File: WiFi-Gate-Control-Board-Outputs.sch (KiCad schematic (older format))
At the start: 47 parts, among them J10 Screw_Terminal_01x02, J11 Screw_Terminal_01x04, J12 Screw_Terminal_01x04, U24 LMZ21700, U25 LP5024, U26 TCA6408A, U27 ITS4075Q

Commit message: Rev 1.0 Release
Added input design and calculations. Added BOM. Added Fuse 3D Model.
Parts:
- C55: renamed from C72; Description CAP, 0603, 1000pF, 10%, X7R, 10V -> CAP, 0603, 1nF, 10%, X7R, 10V
- C56: renamed from C73; Description CAP, 0603, 1000pF, 10%, X7R, 10V -> CAP, 0603, 1nF, 10%, X7R, 10V
- C59: renamed from C76; Description CAP, 0603, 3300pF, 5%, X7R, 10V -> CAP, 0603, 3.3nF, 5%, X7R, 10V
- J9: renamed from J10; Description CON, THT, 5.08mm Pluggable Terminal Strip, 4 Pos -> CON, THT, 5.08mm Pluggable Terminal Strip, 2 Pos
- RL1, RL2: Vendor Part Number 849-CPC1511 -> 849-CPC1511Y
- renumbered C71 to C54, C74 to C57, C75 to C58, C77 to C60, C78 to C61, C79 to C62, C80 to C63, D14 to D13, D15 to D14, D16 to D15, D17 to D16, D18 to D17, D19 to D18, D20 to D19, D21 to D20, D22 to D21, D23 to D22, D24 to D23, D25 to D24, D26 to D25, D27 to D26, D28 to D27, J11 to J10, J12 to J11, R75 to R63, R76 to R64, R77 to R65, R78 to R66, R79 to R67, R80 to R68, R81 to R69, R82 to R70, R83 to R71, R84 to R72, R85 to R73, R86 to R74, U24 to U21, U25 to U22, U26 to U23, U27 to U24

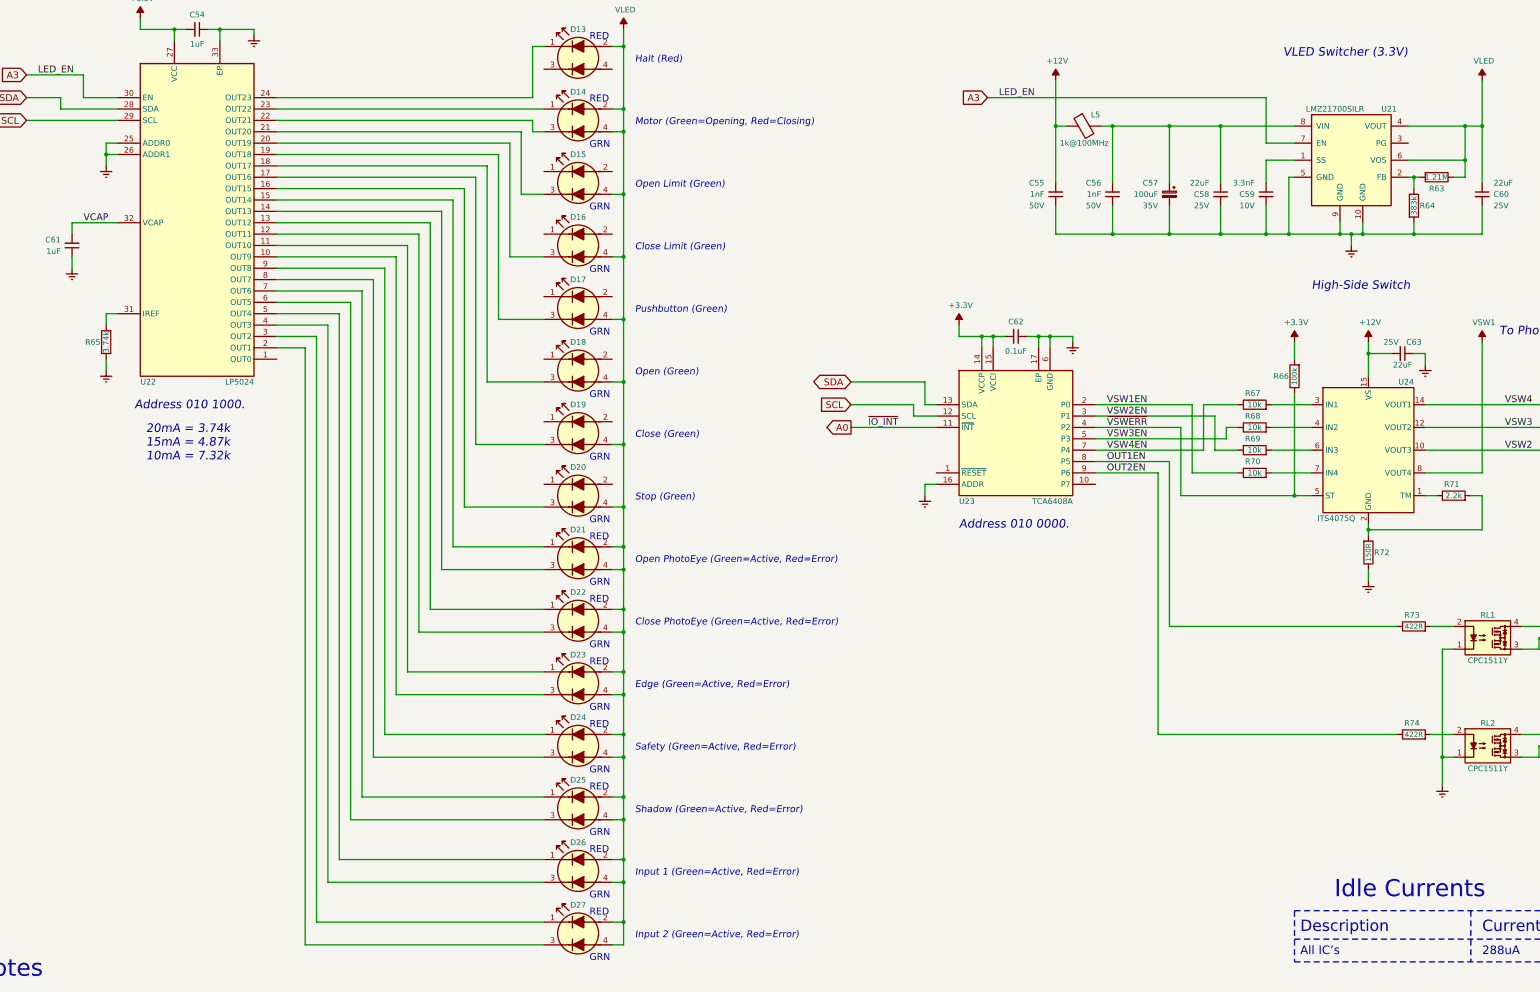
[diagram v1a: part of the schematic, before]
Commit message: PCB to Rev 1.1
Fixed missing Reference Designators on top Silkscreen.
Reset input on TCA6424A and TCA6408A now connected to 3.3V.
Added series Schottky Diode to LED power supply input.
Replaced 1000uF main power capacitor with two 470uF capacitors.
Replaced DS18B20 temperature sensor with TMP100 temperature sensor.
Increased LED currents to 25mA
Removed U26 inverter and connected U3 IN pin directly to processor. Now able to measure unloaded offset current.
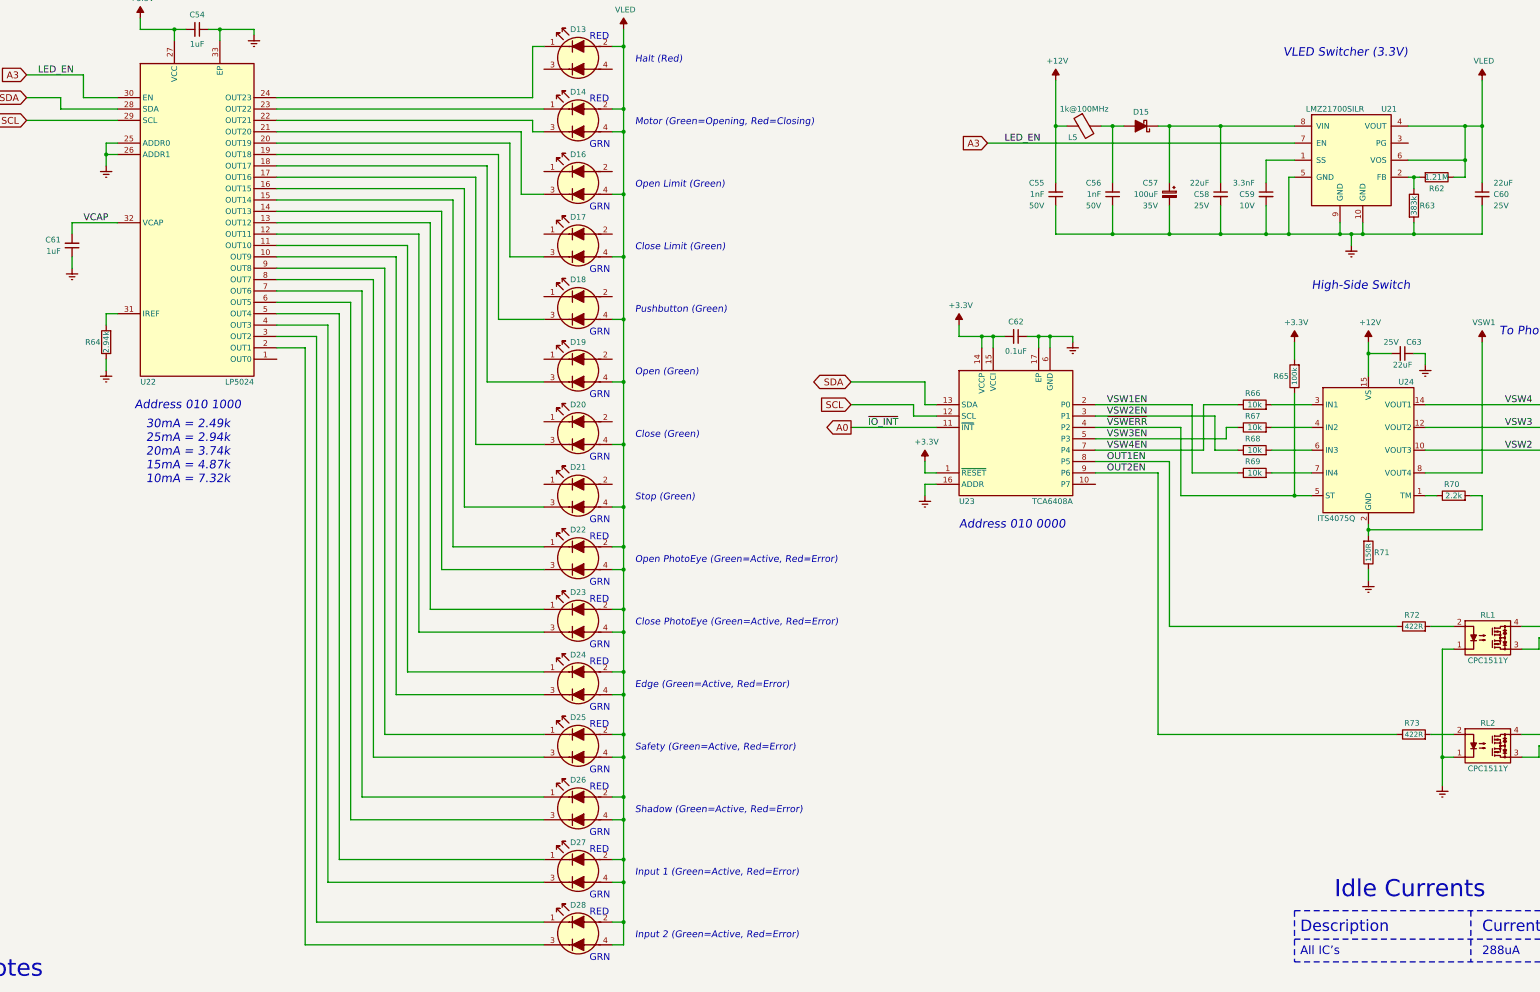
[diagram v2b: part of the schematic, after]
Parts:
- added D15: DFLS130, Diode_SMD:D_PowerDI-123, symbol Device:D_Schottky_ALT
- J10, J11: value Screw_Terminal_01x04 -> Screw Header 4 Pos; Description CON, THT, 5.08mm Pluggable Terminal Strip, 4 Pos -> CON, THT, 5.08mm Pluggable Terminal Header, 4 Pos
- J9: value Screw_Terminal_01x02 -> Screw Header 2 Pos; Description CON, THT, 5.08mm Pluggable Terminal Strip, 2 Pos -> CON, THT, 5.08mm Pluggable Terminal Header, 2 Pos
- R64: renamed from R65; value 3.74k -> 2.94k; Description RES, 0603, 3.74k, 1/10W, 1%, T100 -> RES, 0603, 2.94k, 1/10W, 1%, T100; Part Number ERJ-3EKF3741V -> ERJ-3EKF2941V; Vendor Part Number 667-ERJ-3EKF3741V -> 667-ERJ-3EKF2941V
- R66: renamed from R67; Description RES, 0603, 10k, 1/10W, 1%, T100 -> RES, 0603, 10k, 1/16W, 0.5%, T25; Manufacturer Panasonic -> Susumu; Part Number ERJ-3EKF1002V -> RR0816P-103-D; Tolerance 1% -> 0.5%; Vendor Part Number 667-ERJ-3EKF1002V -> 754-RR0816P-103D
- R67: renamed from R68; Description RES, 0603, 10k, 1/10W, 1%, T100 -> RES, 0603, 10k, 1/16W, 0.5%, T25; Manufacturer Panasonic -> Susumu; Part Number ERJ-3EKF1002V -> RR0816P-103-D; Tolerance 1% -> 0.5%; Vendor Part Number 667-ERJ-3EKF1002V -> 754-RR0816P-103D
- R68: renamed from R69; Description RES, 0603, 10k, 1/10W, 1%, T100 -> RES, 0603, 10k, 1/16W, 0.5%, T25; Manufacturer Panasonic -> Susumu; Part Number ERJ-3EKF1002V -> RR0816P-103-D; Tolerance 1% -> 0.5%; Vendor Part Number 667-ERJ-3EKF1002V -> 754-RR0816P-103D
- R69: renamed from R70; Description RES, 0603, 10k, 1/10W, 1%, T100 -> RES, 0603, 10k, 1/16W, 0.5%, T25; Manufacturer Panasonic -> Susumu; Part Number ERJ-3EKF1002V -> RR0816P-103-D; Tolerance 1% -> 0.5%; Vendor Part Number 667-ERJ-3EKF1002V -> 754-RR0816P-103D
- R70: renamed from R71; Part Number ERJ-3EKF2202V -> ERJ-3EKF2201V; Vendor Part Number 667-ERJ-3EKF2202V -> 667-ERJ-3EKF2201V
- R72: renamed from R73; Description RES, 0603, 42R, 1/10W, 1%, T100 -> RES, 0603, 422R, 1/10W, 1%, T100
- R73: renamed from R74; Description RES, 0603, 42R, 1/10W, 1%, T100 -> RES, 0603, 422R, 1/10W, 1%, T100
- renumbered D15 to D16, D16 to D17, D17 to D18, D18 to D19, D19 to D20, D20 to D21, D21 to D22, D22 to D23, D23 to D24, D24 to D25, D25 to D26, D26 to D27, D27 to D28, R63 to R62, R64 to R63, R66 to R65, R72 to R71
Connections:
- net +3.3V: now also U23.1 (~RESET)
- net at C57.1, C58.1, U21.8 (VIN): now also D15.1 (K); no longer C56.2, L5.2
- new net: C56.2, D15.2 (A), L5.2
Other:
- note added: "30mA = 2.49k\n25mA = 2.94k\n20mA = 3.74k\n15mA = 4.87k\n10mA = 7.32k"
- note added: "Address 010 0000"
- note added: "Address 010 1000"
- note removed: "20mA = 3.74k\n15mA = 4.87k\n10mA = 7.32k"
- note removed: "Address 010 0000."
- note removed: "Address 010 1000."
